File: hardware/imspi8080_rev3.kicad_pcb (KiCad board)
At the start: 2 copper layers, 204 x 95 mm, 91 parts, among them J1 USB_C_Receptacle_USB2.0_16P, J2 USB_C_Receptacle_USB2.0_16P, J3 SW_PADS, J4 SW_PADS, J5 Conn_01x03_Pin, SW1 SW_Push, SW2 SW_Push, U1 RP2040, U2 W25Q128JVS, U3 TLC5947DAP, U4 TLC5947DAP, U5 74HC165, U6 74HC165, U7 Micro_SD_Card, U8 AMS1117-3.3, U9 AMS1117-3.3, Y1 12MHz

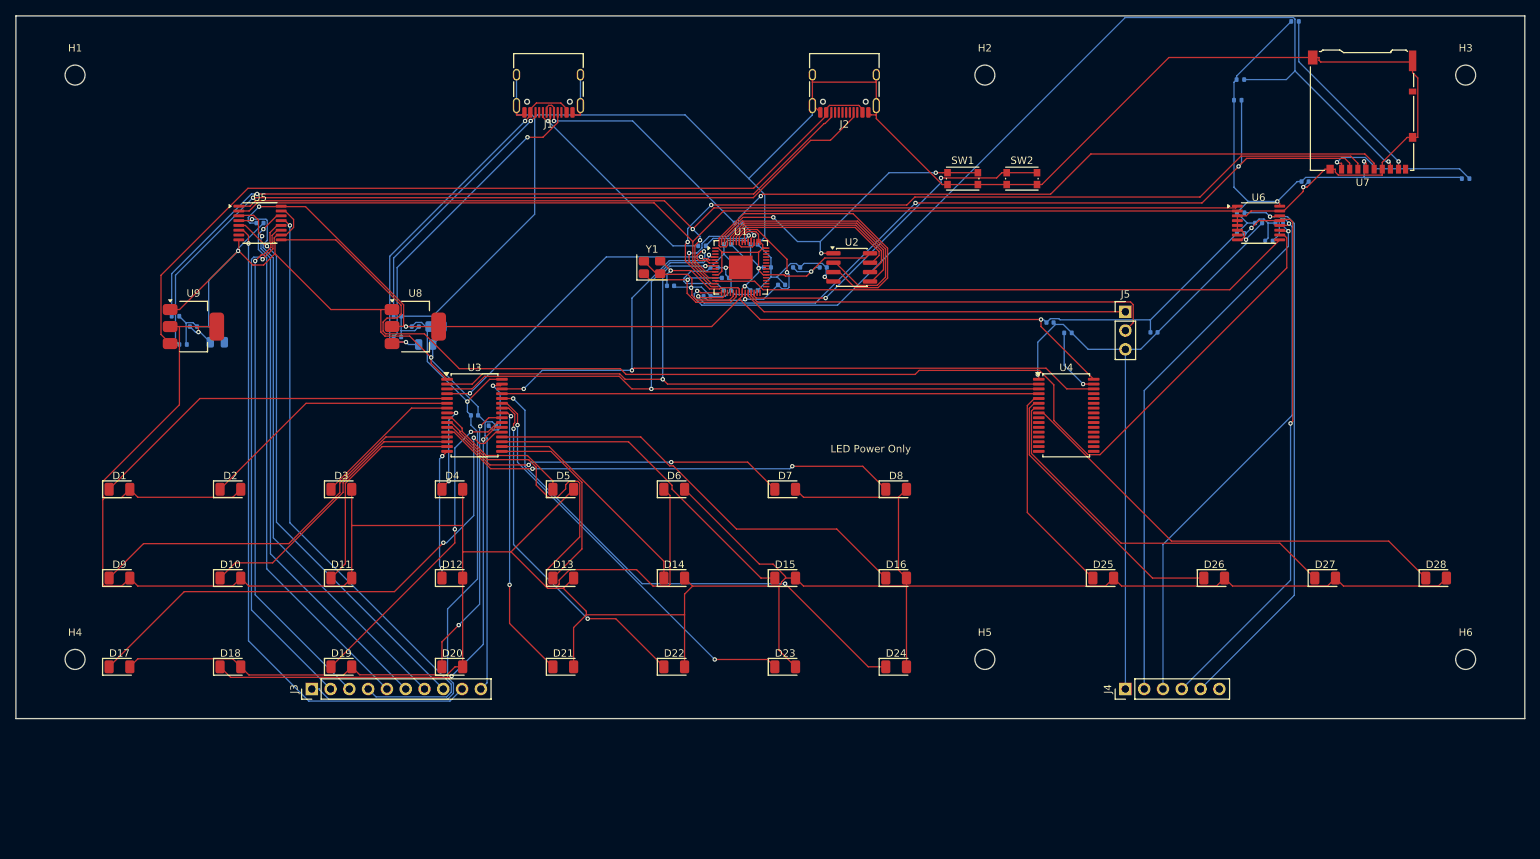
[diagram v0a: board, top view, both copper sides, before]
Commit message: feat(rev3): void-switch design — on-board fascia switches through PCB voids
Reworked rev3 into a signal-flow placement (RP2040 center, one TLC per LED bank,
'165s toward their switch pads) on a 204x112 board. J3/J4 replaced by 12 per-switch
landing-pad clusters (data 1x03, command 2x03) over body voids: fascia-mounted
MTS-123/223 switches drop their bodies through the cutouts (board stays close ->
crisp LEDs), pins jumper to the pads. Back-silk labels every pad (Sn/Cn/V/G) with a
legend; 3V3/GND rails bussed. Fully routed, 0 unconnected (10 track-to-void
clearances remain for the KiCad finish). Build: rev3_place2.py -> rev3_voids.py.

Faceplate updated to 204x112: toggle holes over the voids, LEDs above, masthead +
blue open-bottom frame + rack ear wings. Removed superseded rev3_build.py.

Co-Authored-By: Claude Opus 4.8 (1M context) <noreply@anthropic.com>
Claude-Session: https://claude.ai/code/session_01D2uBTm2rbJxDrjkQXCydg1
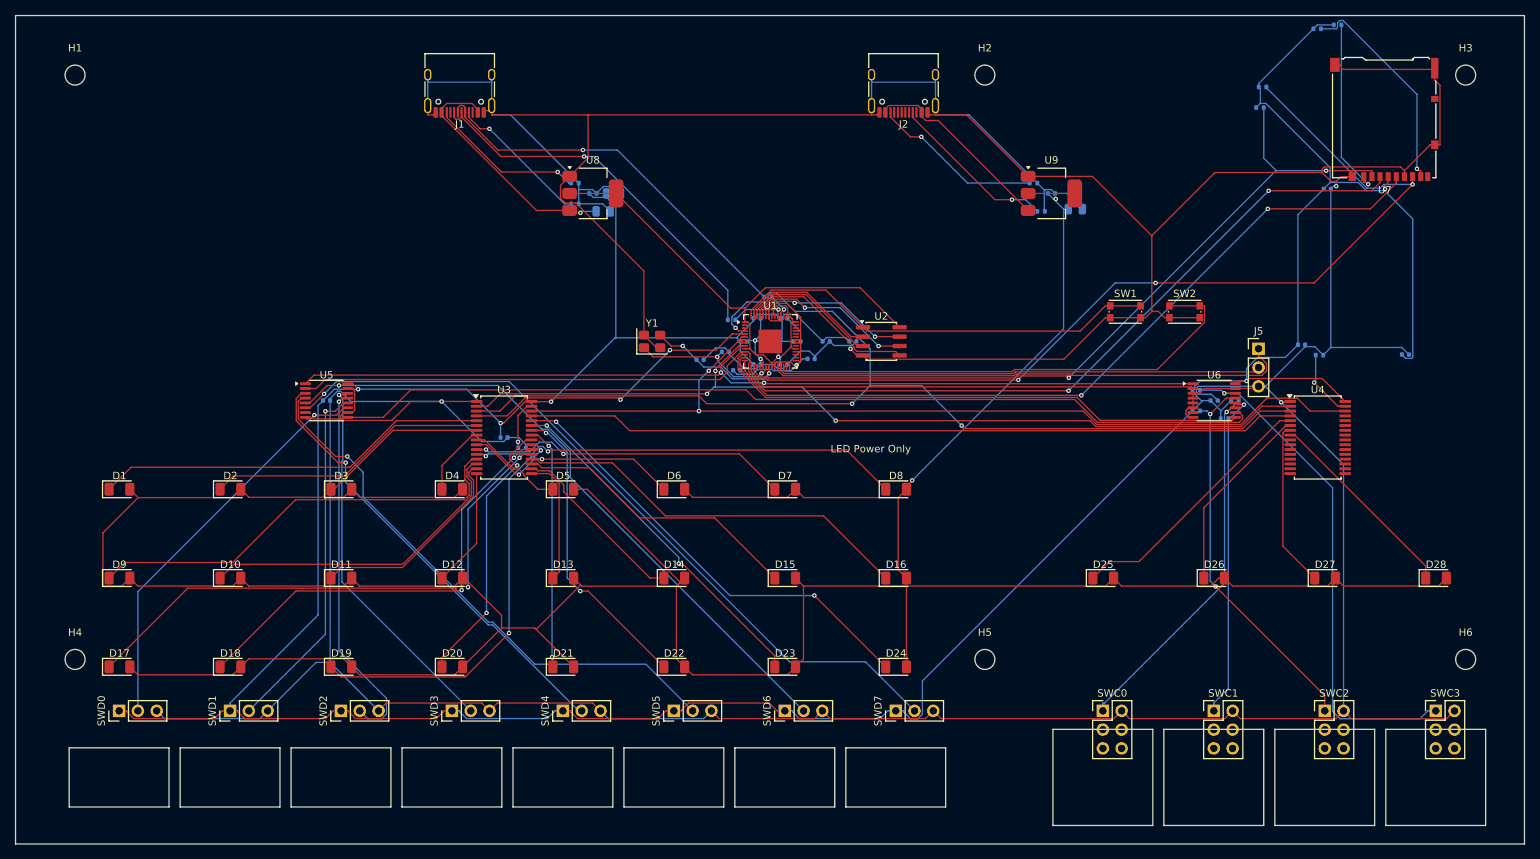
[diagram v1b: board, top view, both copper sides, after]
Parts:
- removed J3: SW_PADS, PinHeader_1x10_P2.54mm_Vertical
- removed J4: SW_PADS, PinHeader_1x06_P2.54mm_Vertical
- added SWC0: SW_LAND, PinHeader_2x03_P2.54mm_Vertical, F.Cu at (182.3, 147.8)
- added SWC1: SW_LAND, PinHeader_2x03_P2.54mm_Vertical, F.Cu at (197.3, 147.8)
- added SWC2: SW_LAND, PinHeader_2x03_P2.54mm_Vertical, F.Cu at (212.3, 147.8)
- added SWC3: SW_LAND, PinHeader_2x03_P2.54mm_Vertical, F.Cu at (227.3, 147.8)
- added SWD0: SW_LAND, PinHeader_1x03_P2.54mm_Vertical, F.Cu at (49.3, 147.8)
- added SWD1: SW_LAND, PinHeader_1x03_P2.54mm_Vertical, F.Cu at (64.3, 147.8)
- added SWD2: SW_LAND, PinHeader_1x03_P2.54mm_Vertical, F.Cu at (79.3, 147.8)
- added SWD3: SW_LAND, PinHeader_1x03_P2.54mm_Vertical, F.Cu at (94.3, 147.8)
- added SWD4: SW_LAND, PinHeader_1x03_P2.54mm_Vertical, F.Cu at (109.3, 147.8)
- added SWD5: SW_LAND, PinHeader_1x03_P2.54mm_Vertical, F.Cu at (124.3, 147.8)
- added SWD6: SW_LAND, PinHeader_1x03_P2.54mm_Vertical, F.Cu at (139.3, 147.8)
- added SWD7: SW_LAND, PinHeader_1x03_P2.54mm_Vertical, F.Cu at (154.3, 147.8)
- moved C14 117.4 mm to (175.4, 77.9)
- moved C21 117.4 mm to (178.6, 80.0)
- moved R3 117.4 mm to (174.0, 80.3)
- moved U9 117.4 mm to (175.4, 77.9)
- moved R4 117.4 mm to (172.9, 76.5)
- moved C18 34.1 mm to (223.2, 99.7)
- moved C8 34.1 mm to (209.2, 98.3)
- moved R8 34.1 mm to (211.6, 99.7)
- moved U4 34.1 mm to (211.4, 110.9)
- moved C13 30.0 mm to (113.4, 77.9)
- moved C20 30.0 mm to (116.2, 77.9)
- moved C22 30.0 mm to (114.8, 80.3)
- moved R1 30.0 mm to (111.0, 79.3)
- moved R2 30.0 mm to (111.0, 76.5)
- moved U8 30.0 mm to (113.4, 77.9)
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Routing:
- net GND: track 572.4 -> 822.8 mm, vias 8 -> 6
- net +3V3: track 398.2 -> 557.9 mm, vias 9 -> 6
- net VBUS_LED: track 115.3 -> 26.4 mm
- net N$5: track 110.7 -> 22.8 mm
- net N$6: track 104.3 -> 23.1 mm
- net HC_CHAIN: track 173.2 -> 126.1 mm
- net N$16: track 72.7 -> 29.5 mm, vias 0 -> 2
- net TLC_SCLK: track 106.4 -> 147.3 mm, vias 2 -> 3
- net SW2: track 85.5 -> 50.6 mm
- net N$38: track 61.6 -> 27.3 mm
- net CMD1: track 76.5 -> 44.5 mm
- net TLC_CHAIN: track 72.6 -> 104.2 mm
- net N$37: track 52.2 -> 22.5 mm
- net +3V3_LED: track 448.8 -> 476.3 mm, vias 1 -> 2
- net CMD2: track 76.8 -> 52.4 mm
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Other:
- board size 204 x 95 mm -> 204 x 112 mm
- board text added: "C0"
- board text added: "C1"
- board text added: "C2"
- board text added: "C3"
- board text added: "G"
- board text added: "S0"
- board text added: "S1"
- board text added: "S2"
- board text added: "S3"
- board text added: "S4"
- board text added: "S5"
- board text added: "S6"
- board text added: "S7"
- board text added: "SWITCH LANDS V=+3V3 G=GND (both bussed) Sn=data common Cn=cmd common"
- board text added: "V"

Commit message: feat(rev3): landing-pad switch design + fab package; archive void detour
Replaced the switch-through-void design (un-solderable: pins ended up behind the
switch body with no reachable pad) with a solderable landing-pad scheme: switches
mount on the fascia just below the board's bottom edge and jumper straight up to a
labeled pad cluster each (SWD0-7 data 1x3, SWC0-3 command 2x3; back-silk V/Sn/G,
Cn/G). No voids, no connectors, no cables. Board 204x99.7, fully routed, DRC-clean
(0 unconnected, 0 errors). Build chain: rev3_place2.py -> rev3_pads.py.

Added jlcpcb-rev3/ upload package: gerbers.zip (copper/mask/silk/paste + PTH/NPTH
drill), CPL (83 SMT parts), BoM (electronics only; switch lands hand-jumpered),
README. Faceplate regenerated for the 98mm board (toggle holes below the LEDs).

Repo hygiene so vendor upload is unambiguous: jlcpcb-rev3/ is the only current
package; archived the void scripts (rev3_voids.py, rev3_back.png) and renamed the
old rev1 package (jlcpcb -> jlcpcb-rev1) under OLD/. README points at the one folder.

Co-Authored-By: Claude Opus 4.8 (1M context) <noreply@anthropic.com>
Claude-Session: https://claude.ai/code/session_01D2uBTm2rbJxDrjkQXCydg1
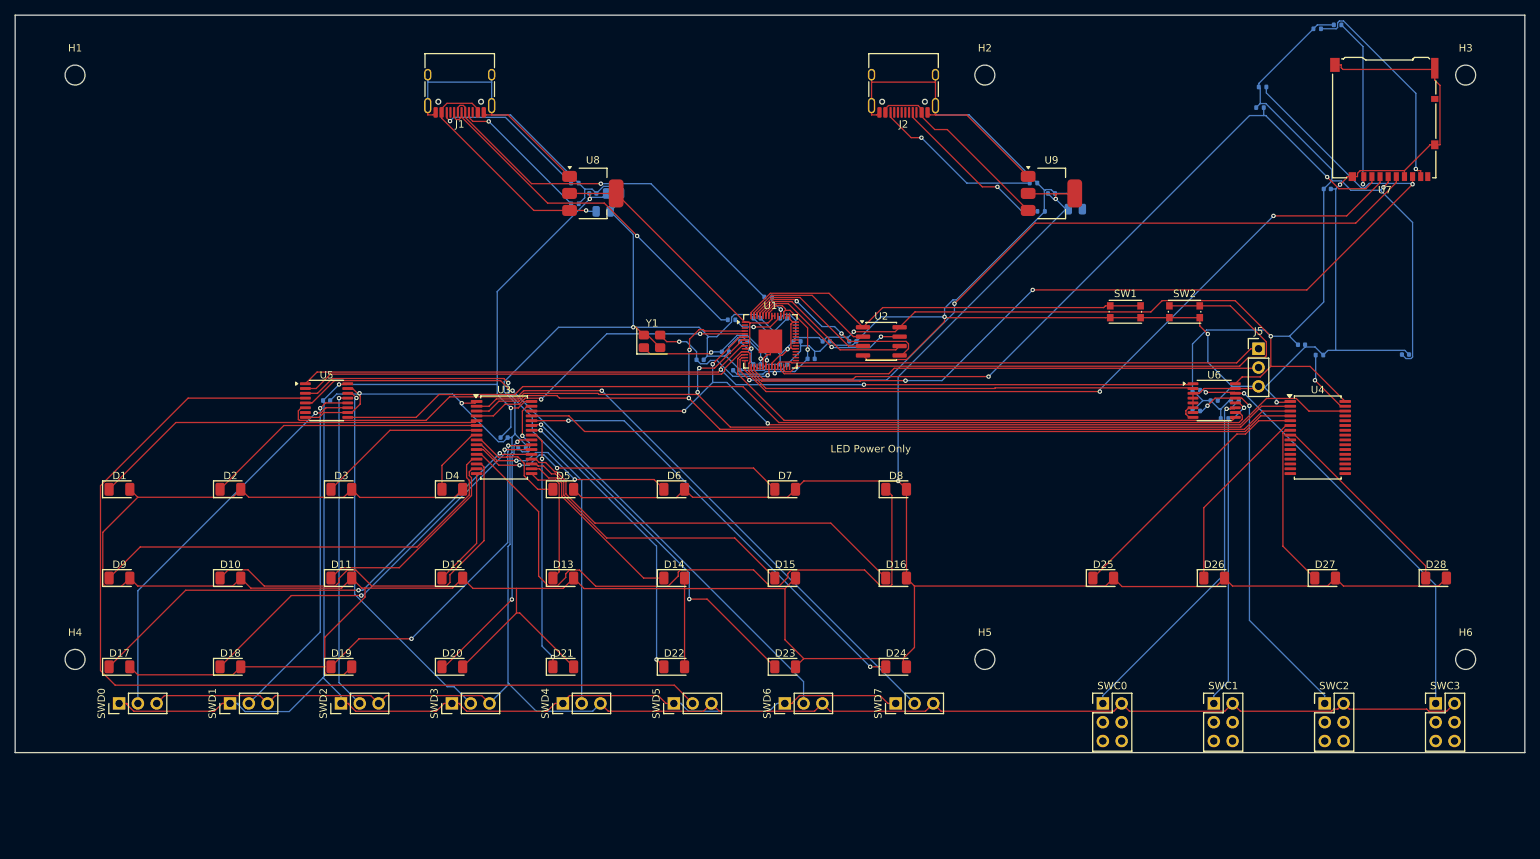
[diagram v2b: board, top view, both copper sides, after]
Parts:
- moved SWC0 1.00 mm to (182.3, 146.8)
- moved SWC1 1.00 mm to (197.3, 146.8)
- moved SWC2 1.00 mm to (212.3, 146.8)
- moved SWC3 1.00 mm to (227.3, 146.8)
- moved SWD0 1.00 mm to (49.3, 146.8)
- moved SWD1 1.00 mm to (64.3, 146.8)
- moved SWD2 1.00 mm to (79.3, 146.8)
- moved SWD3 1.00 mm to (94.3, 146.8)
- moved SWD4 1.00 mm to (109.3, 146.8)
- moved SWD5 1.00 mm to (124.3, 146.8)
- moved SWD6 1.00 mm to (139.3, 146.8)
- moved SWD7 1.00 mm to (154.3, 146.8)
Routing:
- net GND: track 822.8 -> 722.8 mm, vias 6 -> 8
- net SW5: track 75.2 -> 139.5 mm, vias 1 -> 0
- net +3V3: track 557.9 -> 512.9 mm, vias 6 -> 8
- net N$18: track 58.5 -> 88.3 mm, vias 2 -> 0
- net TLC_SCLK: track 147.3 -> 129.9 mm, vias 3 -> 2
- net RUN: track 67.1 -> 83.7 mm
- net SW4: track 60.9 -> 75.9 mm
- net CMD3: track 69.9 -> 58.8 mm, vias 1 -> 2
- net N$20: track 44.0 -> 53.4 mm
- net N$29: track 55.5 -> 47.2 mm
- net SW2: track 50.6 -> 43.6 mm
- net VCORE: track 30.9 -> 24.7 mm, vias 1 -> 2
- net N$27: track 75.3 -> 69.1 mm
- net N$28: track 60.6 -> 54.6 mm
- net N$1: track 70.8 -> 66.4 mm
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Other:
- board size 204 x 112 mm -> 204.1 x 99.7 mm
- board text added: "SWITCH LANDS (below-board) V=+3V3 G=GND (bussed) Sn=data common Cn=cmd common"
- board text removed: "SWITCH LANDS V=+3V3 G=GND (both bussed) Sn=data common Cn=cmd common"
